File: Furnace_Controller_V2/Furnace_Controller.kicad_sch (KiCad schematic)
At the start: 18 parts, among them J1 Power In Treminal, J3 Relay Terminal, J4 HMD Terminal, J5 RS-485 Terminal, Q5 2n2222

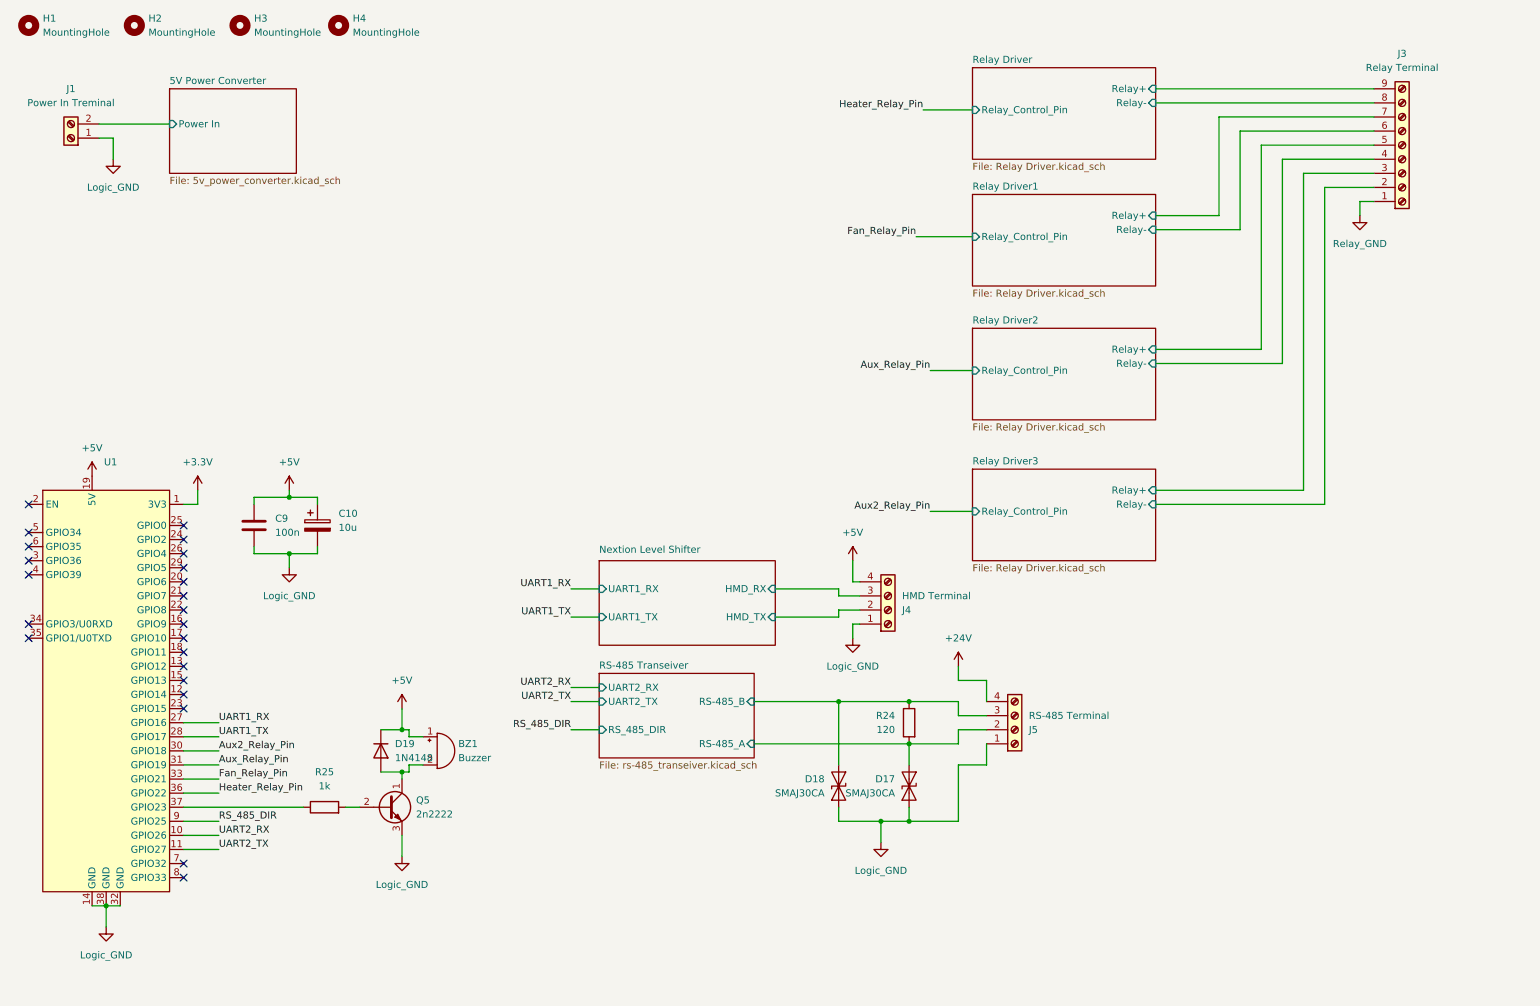
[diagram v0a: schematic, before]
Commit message: Organize PCB revisions and correct TI footprints
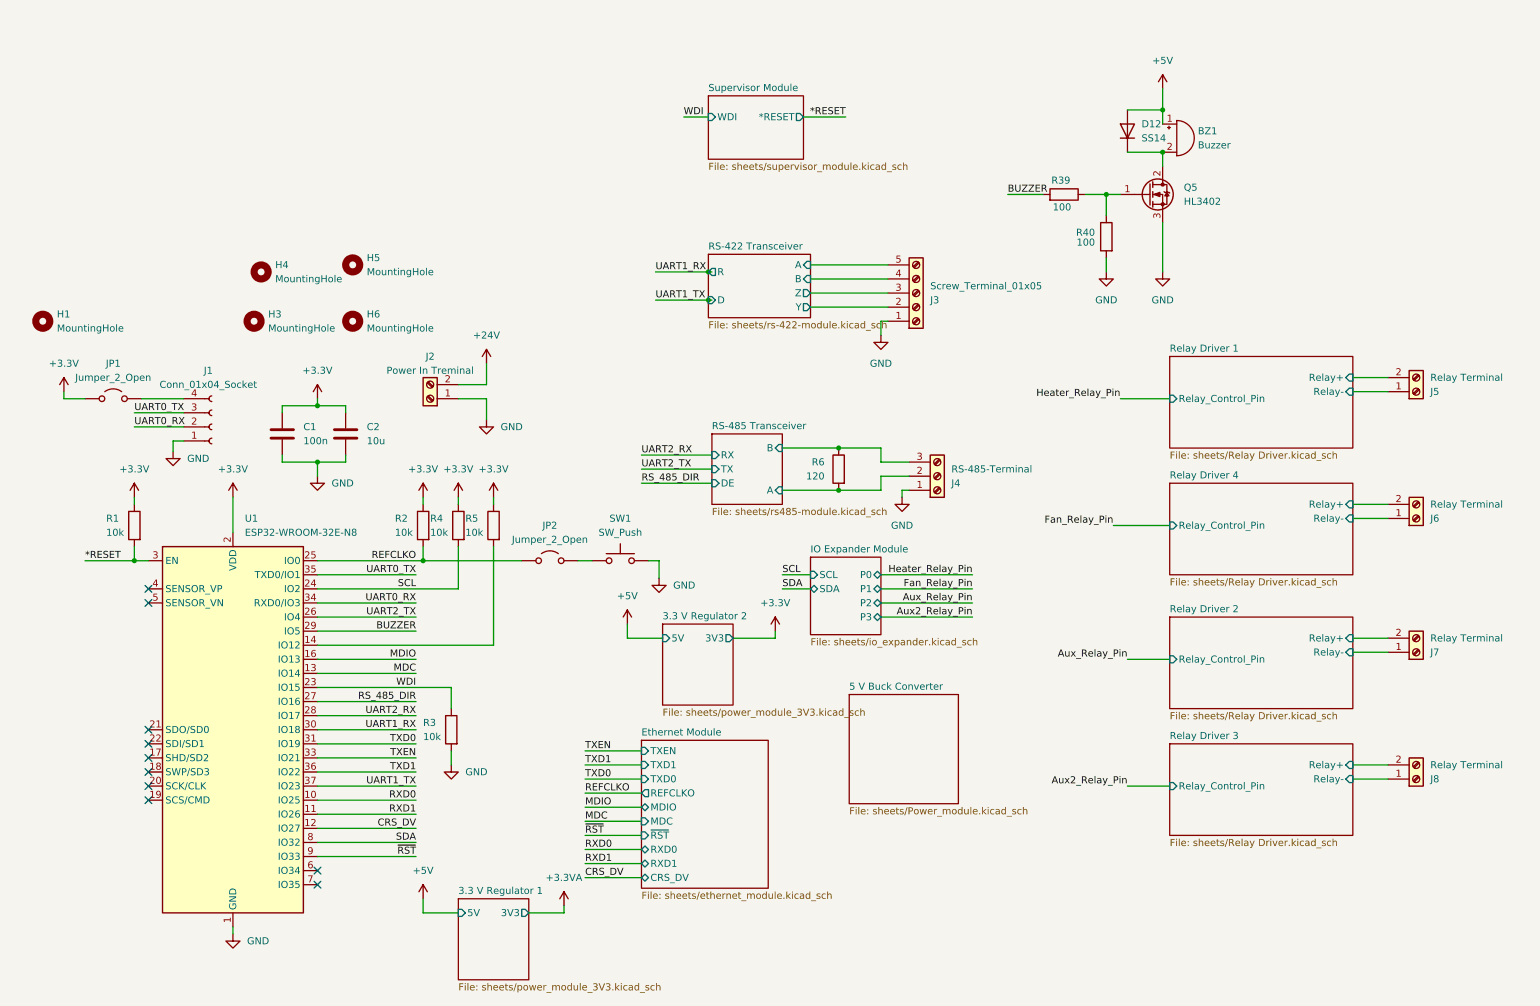
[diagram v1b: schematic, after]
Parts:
- removed C10: 10u, Capacitor_THT:CP_Radial_D5.0mm_P2.00mm, symbol Device:C_Polarized
- removed D17, D18: SMAJ30CA, Diode_SMD:D_SMA, symbol Diode:SMAJ30CA
- removed D19: 1N4148, Diode_THT:D_DO-35_SOD27_P7.62mm_Horizontal, symbol Diode:1N4148
- removed H2: MountingHole, MountingHole:MountingHole_5.3mm_M5, symbol Mechanical:MountingHole
- removed J3: Relay Terminal, TerminalBlock:TerminalBlock_MaiXu_MX126-5.0-09P_1x09_P5.00mm, symbol Connector:Screw_Terminal_01x09
- removed J4: HMD Terminal, TerminalBlock:TerminalBlock_MaiXu_MX126-5.0-04P_1x04_P5.00mm, symbol Connector:Screw_Terminal_01x04
- removed J5: RS-485 Terminal, TerminalBlock:TerminalBlock_MaiXu_MX126-5.0-04P_1x04_P5.00mm, symbol Connector:Screw_Terminal_01x04
- removed Q5: 2n2222, Package_TO_SOT_THT:TO-92_Inline, symbol Transistor_BJT:BC337
- removed R25: 1k, Resistor_SMD:R_0805_2012Metric_Pad1.20x1.40mm_HandSolder, symbol Device:R
- removed U1: ~, Custom_Footprints:ESP32_DevKitc_V4, symbol Custom_Symbols:ESP32_DevKitc_V4
- added C2: 10u, Capacitor_SMD:C_0805_2012Metric, symbol Device:C
- added D12: SS14, Diode_SMD:D_SOD-123, symbol Device:D
- added H4: MountingHole, MountingHole:MountingHole_3.2mm_M3, symbol Mechanical:MountingHole
- added H5: MountingHole, MountingHole:MountingHole_2.2mm_M2, symbol Mechanical:MountingHole
- added J1: Conn_01x04_Socket, Connector_PinHeader_2.54mm:PinHeader_1x04_P2.54mm_Vertical, symbol Connector:Conn_01x04_Socket
- added J3: Screw_Terminal_01x05, Connector_Phoenix_MC:PhoenixContact_MC_1,5_5-G-3.5_1x05_P3.50mm_Horizontal, symbol Connector:Screw_Terminal_01x05
- added J4: RS-485-Terminal, Connector_Phoenix_MC:PhoenixContact_MC_1,5_3-G-3.5_1x03_P3.50mm_Horizontal, symbol Connector:Screw_Terminal_01x03
- added J5, J6, J7, J8: Relay Terminal, Connector_Phoenix_MC:PhoenixContact_MC_1,5_2-G-3.5_1x02_P3.50mm_Horizontal, symbol Connector:Screw_Terminal_01x02
- added JP1, JP2: Jumper_2_Open, TestPoint:TestPoint_2Pads_Pitch2.54mm_Drill0.8mm, symbol Jumper:Jumper_2_Open
- added Q5: HL3402, PCM_JLCPCB:Q_SOT-23, symbol Transistor_FET:IRLZ44N
- added R1, R2, R3, R4, R5: 10k, Resistor_SMD:R_0603_1608Metric, symbol Device:R
- added R39, R40: 100, Resistor_SMD:R_0603_1608Metric, symbol Device:R
- added SW1: SW_Push, Button_Switch_THT:SW_PUSH_6mm_H4.3mm, symbol Switch:SW_Push
- added U1: ESP32-WROOM-32E-N8, RF_Module:ESP32-WROOM-32, symbol RF_Module:ESP32-WROOM-32
- C1: renamed from C9; footprint Capacitor_SMD:C_0805_2012Metric_Pad1.18x1.45mm_HandSolder -> Capacitor_SMD:C_0603_1608Metric
- H1, H3: footprint MountingHole:MountingHole_5.3mm_M5 -> MountingHole:MountingHole_3.2mm_M3
- H6: renamed from H4; footprint MountingHole:MountingHole_5.3mm_M5 -> MountingHole:MountingHole_3.2mm_M3
- J2: renamed from J1; footprint TerminalBlock:TerminalBlock_MaiXu_MX126-5.0-02P_1x02_P5.00mm -> Connector_Phoenix_MC:PhoenixContact_MC_1,5_2-G-3.5_1x02_P3.50mm_Horizontal
- R6: renamed from R24; footprint Resistor_SMD:R_0805_2012Metric_Pad1.20x1.40mm_HandSolder -> Resistor_SMD:R_0603_1608Metric
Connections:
- net 5V Power Converter/Power In is gone; now on net +24V: J2.2 (Pin_2)
- net +3.3V: now also C1.1, C2.1, JP1.1 (A), R1.1, R2.1, R4.1, R5.1, U1.2 (VDD)
- net +5V: now also D12.2 (A); no longer C1.1
- net RS_485_DIR: now also U1.27 (IO16)
- net Relay Driver 1/Relay+: now also J5.2 (Pin_2)
- net Relay Driver 1/Relay-: now also J5.1 (Pin_1)
- net Relay Driver 4/Relay+: now also J6.2 (Pin_2)
- net Relay Driver 4/Relay-: now also J6.1 (Pin_1)
- net Relay Driver 2/Relay+: now also J7.2 (Pin_2)
- net Relay Driver 2/Relay-: now also J7.1 (Pin_1)
- net Relay Driver 3/Relay+: now also J8.2 (Pin_2)
- net Relay Driver 3/Relay-: now also J8.1 (Pin_1)
- net UART1_RX: now also U1.30 (IO18)
- net UART1_TX: now also U1.37 (IO23)
- net UART2_RX: now also U1.28 (IO17)
- net UART2_TX: now also U1.26 (IO4)
- net at BZ1.2 (-): now also D12.1 (K), Q5.2 (D)
- net Logic_GND renamed GND
- net GND: now also C2.2, J1.1 (Pin_1), J3.1 (Pin_1), J4.1 (Pin_1), Q5.3 (S), R3.2, R40.2, SW1.2, U1.1 (GND), U1.15 (GND), U1.38 (GND), U1.39 (GND)
- net RS-485 Transeiver/RS-485_A renamed RS-485 Transceiver/A
- net RS-485 Transceiver/A: now also J4.2 (Pin_2)
- net RS-485 Transeiver/RS-485_B renamed RS-485 Transceiver/B
- net RS-485 Transceiver/B: now also J4.3 (Pin_3)
- new net: J1.4 (Pin_4), JP1.2 (B)
- new net: R5.2, U1.14 (IO12)
- new net: Q5.1 (G), R39.1, R40.1
- new net: JP2.2 (B), SW1.1
- new net *RESET: R1.2, U1.3 (EN)
- new net BUZZER: R39.2, U1.29 (IO5)
- new net CRS_DV: U1.12 (IO27)
- new net MDC: U1.13 (IO14)
- new net MDIO: U1.16 (IO13)
- new net REFCLKO: JP2.1 (A), R2.2, U1.25 (IO0)
- new net RS-422 Transceiver/A: J3.5 (Pin_5)
- new net RS-422 Transceiver/B: J3.4 (Pin_4)
- new net RS-422 Transceiver/Y: J3.2 (Pin_2)
- new net RS-422 Transceiver/Z: J3.3 (Pin_3)
- new net RXD0: U1.10 (IO25)
- new net RXD1: U1.11 (IO26)
- new net SCL: R4.2, U1.24 (IO2)
- new net SDA: U1.8 (IO32)
- new net TXD0: U1.31 (IO19)
- new net TXD1: U1.36 (IO22)
- new net TXEN: U1.33 (IO21)
- new net UART0_RX: J1.2 (Pin_2), U1.34 (RXD0/IO3)
- new net UART0_TX: J1.3 (Pin_3), U1.35 (TXD0/IO1)
- new net WDI: R3.1, U1.23 (IO15)
- new net ~{RST}: U1.9 (IO33)
- no-connect marks 23 -> 10
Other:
- sheet Relay Driver renamed Relay Driver 1
- sheet Relay Driver1 renamed Relay Driver 4
- sheet Relay Driver2 renamed Relay Driver 2
- sheet Relay Driver3 renamed Relay Driver 3
- removed sheet 5V Power Converter
- removed sheet Nextion Level Shifter
- removed sheet RS-485 Transeiver
- added sheet 3.3 V Regulator 1 (sheets/power_module_3V3.kicad_sch)
- added sheet 3.3 V Regulator 2 (sheets/power_module_3V3.kicad_sch)
- added sheet 5 V Buck Converter (sheets/Power_module.kicad_sch)
- added sheet Ethernet Module (sheets/ethernet_module.kicad_sch)
- added sheet IO Expander Module (sheets/io_expander.kicad_sch)
- added sheet RS-422 Transceiver (sheets/rs-422-module.kicad_sch)
- added sheet RS-485 Transceiver (sheets/rs485-module.kicad_sch)
- added sheet Supervisor Module (sheets/supervisor_module.kicad_sch)
- sheet Relay Driver 1: file Relay Driver.kicad_sch -> sheets/Relay Driver.kicad_sch
- sheet Relay Driver 2: file Relay Driver.kicad_sch -> sheets/Relay Driver.kicad_sch
- sheet Relay Driver 3: file Relay Driver.kicad_sch -> sheets/Relay Driver.kicad_sch
- sheet Relay Driver 4: file Relay Driver.kicad_sch -> sheets/Relay Driver.kicad_sch
- moved on the sheet: C1, H1, H3, H6, J2, R6

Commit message: Normalize 3.3V net names
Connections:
- net +3.3V renamed +3V3
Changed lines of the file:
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@@
 			)
 		)
-		(property "Value" "+3.3VA"
+		(property "Value" "+3V3A"
 			(at 114.3 168.91 0)
 			(show_name no)
@@
 			)
 		)
-		(property "Value" "+3.3V"
+		(property "Value" "+3V3"
 			(at 24.13 76.2 0)
 			(show_name no)
@@
 			)
 		)
-		(property "Value" "+3.3V"
+		(property "Value" "+3V3"
 			(at 36.83 95.25 0)
 			(show_name no)
@@
 			)
 		)
-		(property "Value" "+3.3V"
+		(property "Value" "+3V3"
 			(at 95.25 95.25 0)
 			(show_name no)
@@
 			)
 		)
-		(property "Value" "+3.3V"
+		(property "Value" "+3V3"
 			(at 88.9 95.25 0)
 			(show_name no)
@@
 			)
 		)
-		(property "Value" "+3.3V"
+		(property "Value" "+3V3"
 			(at 69.85 77.47 0)
 			(show_name no)
@@
 			)
 		)
-		(property "Value" "+3.3V"
+		(property "Value" "+3V3"
 			(at 101.6 95.25 0)
 			(show_name no)
@@
 			)
 		)
-		(property "Value" "+3.3V"
+		(property "Value" "+3V3"
 			(at 152.4 119.38 0)
 			(show_name no)
@@
 			)
 		)
-		(property "Value" "+3.3V"
+		(property "Value" "+3V3"
 			(at 54.61 95.25 0)
 			(show_name no)
